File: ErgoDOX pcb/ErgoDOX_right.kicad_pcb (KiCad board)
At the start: 2 copper layers, 182.8 x 158.9 mm, 97 parts, among them J1 AudioJack4, J2 USB_B_Micro, SW0:10 SW0:3, SW0:11 SW0:2, SW0:12 SW0:1, SW0:7 SW0:6, SW0:8 SW0:5, SW0:9 SW0:4, SW1 TS-1187A-B-A-B, SW1:10 SW1:3, SW1:11 SW1:2, SW1:12 SW1:1, SW1:13 SW1:0, SW1:9 SW1:4, SW2:10 SW2:3, SW2:11 SW2:2, SW2:12 SW2:1, SW2:13 SW2:0, SW2:7 SW2:6, SW2:8 SW2:5, SW2:9 SW2:4, SW3:10 SW3:3, SW3:11 SW3:2, SW3:12 SW3:1, SW3:13 SW3:0, SW3:8 SW3:5, SW3:9 SW3:4, SW4:10 SW4:3, SW4:11 SW4:2, SW4:12 SW4:1, SW4:13 SW4:0, SW4:7 SW4:6, SW4:8 SW4:5, SW4:9 SW4:4, SW5:10 SW5:3, SW5:11 SW5:2, SW5:12 SW5:1, SW5:13 SW5:0, SW5:7 SW5:6, SW5:8 SW5:5, SW5:9 SW5:4, U1 ATmega32U4-MU, U2 MCP23018

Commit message: Routed RH board
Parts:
- removed J2: USB_B_Micro, Connectors_USB:USB_Micro-B_Wuerth-629105150521
- removed LED_C1: LED, LEDs:LED_0603
- removed R1, R2: 22, Resistors_SMD:R_0603
- removed R10, R9: 0, Resistors_SMD:R_0603
- removed R8: 1k, Resistors_SMD:R_0603
- removed SW1: TS-1187A-B-A-B, Buttons_Switches_THT:SW_PUSH_6mm
- removed U1: ATmega32U4-MU, Housings_DFN_QFN:QFN-44-1EP_7x7mm_Pitch0.5mm
- added C4: 1u, Capacitors_SMD:C_0603, F.Cu at (128.0, 45.5)
- added C5: 100n, Capacitors_SMD:C_0603, F.Cu at (102.0, 44.5)
- added C6: 100n, Capacitors_SMD:C_0603, F.Cu at (125.5, 35.9)
- moved R7 164.2 mm to (85.0, 44.5)
- moved R6 153.5 mm to (98.3, 44.5)
- moved U2 123.7 mm to (121.9, 42.1), turned to 90 degrees
- moved LED_B1 84.8 mm to (138.3, 35.5), turned to 180 degrees
- moved D2:12 75.7 mm to (175.6, 132.5)
- moved LED_A1 71.4 mm to (138.3, 37.5), turned to 180 degrees
- moved D2:13 70.6 mm to (184.3, 115.5)
- moved D0:12 56.8 mm to (101.3, 158.5), turned to 180 degrees
- moved R3 35.9 mm to (134.3, 37.5), turned to 0 degrees
- moved D0:11 35.4 mm to (101.3, 154.5)
- moved R4 34.9 mm to (134.3, 35.5), turned to 0 degrees
- moved D2:7 13.6 mm to (68.3, 106.5), turned to 0 degrees
- moved D0:8 11.8 mm to (71.3, 133.5), turned to 205 degrees
- moved D0:10 8.54 mm to (101.3, 150.5), turned to 180 degrees
- moved D1:7 6.23 mm to (51.8, 146.8), turned to 25 degrees
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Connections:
- U2 pad 10: /LED_A -> VCC
- U2 pad 11: VCC -> /SCL
- U2 pad 12: /SCL -> /SDA
- U2 pad 13: /SDA -> GND
- U2 pad 14: (no net) -> VCC
- U2 pad 15: GND -> (no net)
- U2 pad 16: VCC -> (no net)
- U2 pad 17: (no net) -> /COL0
- U2 pad 18: (no net) -> /COL1
- U2 pad 19: (no net) -> /COL11
- U2 pad 2: (no net) -> /ROW5
- U2 pad 20: /COL0 -> /COL10
- U2 pad 21: /COL1 -> /COL4
- U2 pad 22: /COL11 -> /COL5
- U2 pad 23: /COL10 -> /COL6
- U2 pad 24: /COL4 -> (no net)
- U2 pad 3: /ROW5 -> /ROW4
- U2 pad 4: /ROW4 -> /ROW3
- U2 pad 5: /ROW3 -> /ROW2
- U2 pad 6: /ROW2 -> /ROW1
- U2 pad 7: /ROW1 -> /ROW0
- U2 pad 8: /ROW0 -> /LED_B
- U2 pad 9: /LED_B -> /LED_A
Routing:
- net /COL1: track 0.00 -> 225.4 mm
- net /COL10: track 0.00 -> 183.7 mm
- net /COL6: track 0.00 -> 181.3 mm
- net /COL4: track 0.00 -> 170.9 mm
- net /COL11: track 0.00 -> 156.6 mm
- net /COL0: track 0.00 -> 151.8 mm
- net /COL5: track 0.00 -> 131.5 mm
- net /ROW1: track 156.2 -> 250.1 mm
- net VCC: track 0.00 -> 76.9 mm, vias 0 -> 2
- net /ROW3: track 91.5 -> 165.2 mm
- net Net-(D0:12-Pad2): track 0.90 -> 62.1 mm
- net /ROW4: track 121.7 -> 179.9 mm
- net Net-(D0:11-Pad2): track 0.00 -> 45.4 mm
- net /SCL: track 0.00 -> 43.6 mm, vias 0 -> 1
- net /ROW0: track 269.4 -> 231.0 mm, vias 1 -> 0
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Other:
- board size 182.8 x 158.9 mm -> 182.8 x 157.1 mm
- board text removed: "LEFT HAND"
- board text removed: "ProfetKeyboards.com"
- board text removed: "RIGHT HAND"

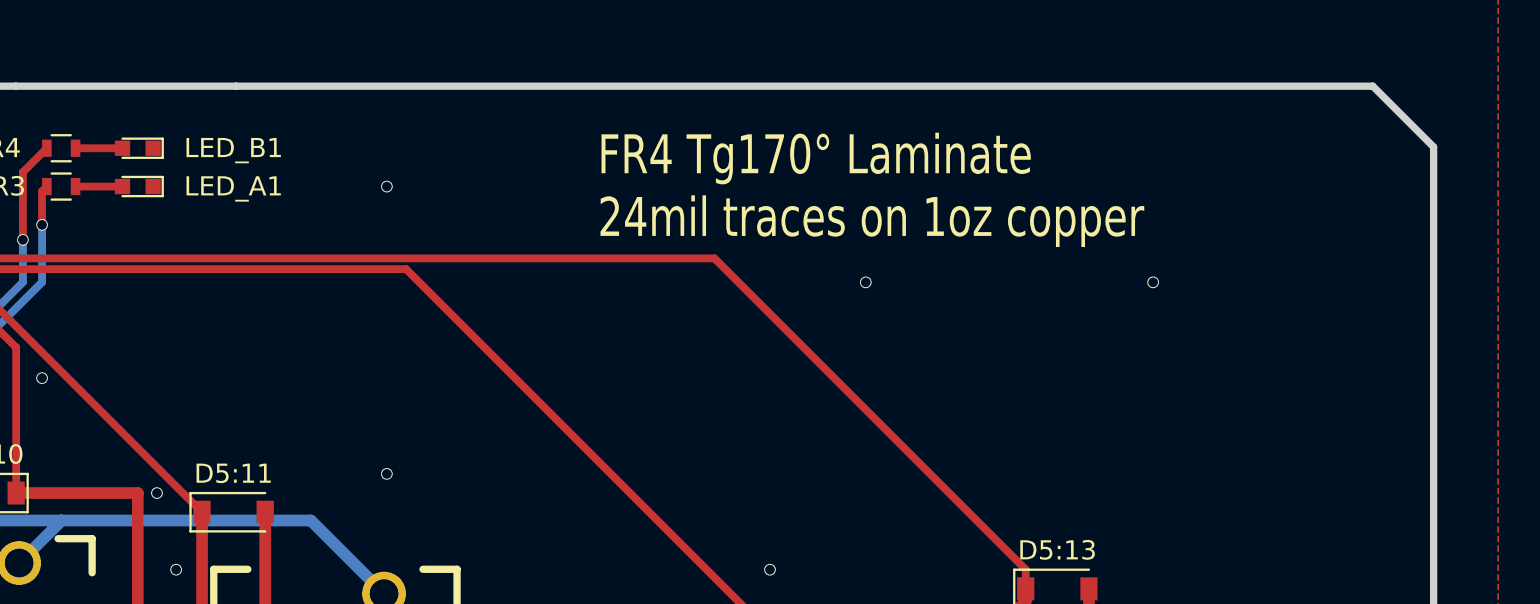
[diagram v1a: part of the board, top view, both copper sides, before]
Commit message: Added revision, generated gerbers
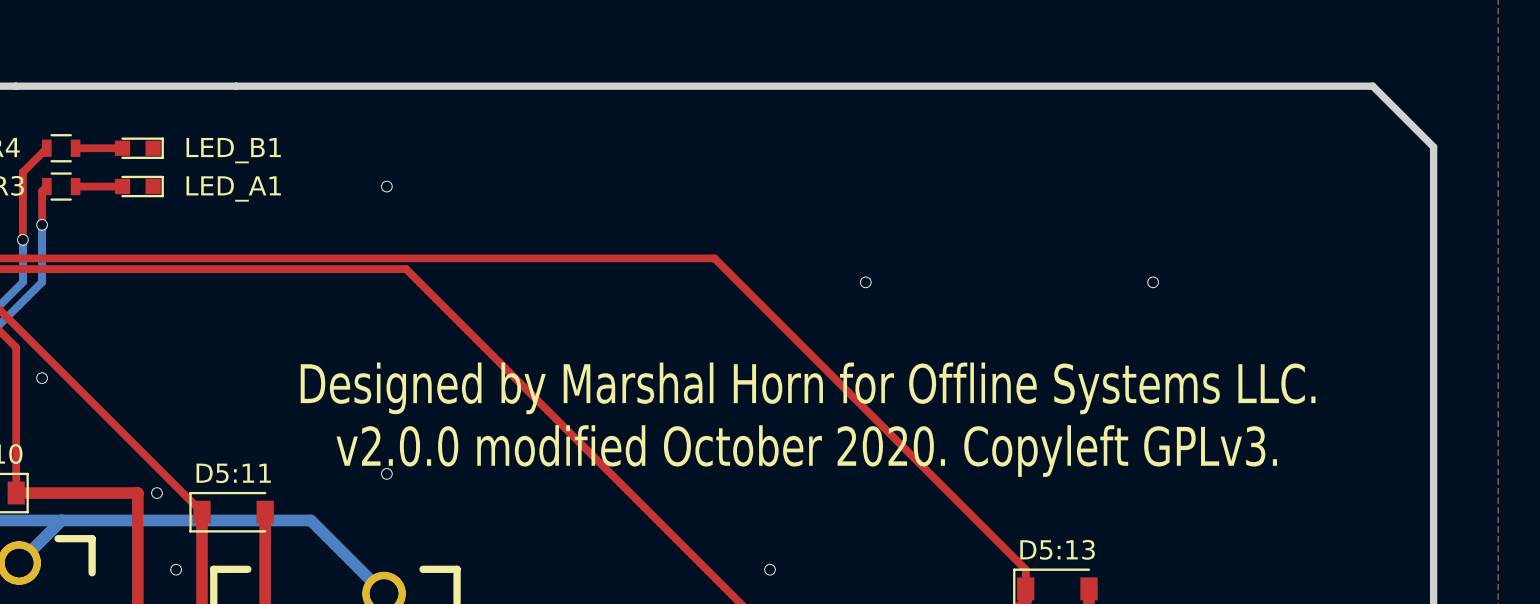
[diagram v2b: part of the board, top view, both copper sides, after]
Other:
- rule pad_to_mask_clearance: 0.0508 -> 0
- board text added: "Designed by Marshal Horn for Offline Systems LLC. v2.0.0 modified October 2020. Copyleft GPLv3."
- board text removed: "FR4 Tg170° Laminate 24mil traces on 1oz copper"
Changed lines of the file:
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@@
   (general
     (thickness 1.6002)
-    (drawings 22)
+    (drawings 21)
     (tracks 467)
     (zones 0)
@@
   )
   (page A4)
+  (title_block
+    (title "ErgoDox Right PCB")
+    (date 2020-10-12)
+    (rev 2.0.0)
+    (company "Offline Systems")
+  )
   (layers
     (0 Front signal)
@@
     (pad_size 0.8 0.8)
     (pad_drill 0.5)
-    (pad_to_mask_clearance 0.0508)
-    (solder_mask_min_width 0.101)
+    (pad_to_mask_clearance 0)
     (aux_axis_origin 0 0)
     (grid_origin 176.276 47.498)
     (visible_elements 7FFFFF7F)
     (pcbplotparams
-      (layerselection 0x01fff_ffffffff)
+      (layerselection 0x0dfff_ffffffff)
       (usegerberextensions true)
       (usegerberattributes true)
       (usegerberadvancedattributes true)
       (creategerberjobfile true)
-      (excludeedgelayer true)
+      (excludeedgelayer false)
       (linewidth 0.150000)
       (plotframeref false)
@@
       (drillshape 0)
       (scaleselection 1)
-      (outputdirectory "gerber/"))
+      (outputdirectory "gerber_right/"))
   )
   (net 0 "")
@@
     )
   )
+  (gr_text "Designed by Marshal Horn for Offline Systems LLC.\nv2.0.0 modified October 2020. Copyleft GPLv3." (at 173.276 49.498) (layer F.SilkS)
+    (effects (font (size 2.032 1.524) (thickness 0.3048)))
+  )
   (gr_line (start 90.121 32.258) (end 93.521 32.258) (layer Edge.Cuts) (width 0.381))
   (gr_line (start 90.121 32.258) (end 77.8764 32.258) (layer Edge.Cuts) (width 0.381))
@@
     (effects (font (size 8.128 12.192) (thickness 2.032)) (justify mirror))
   )
-  (gr_text "FR4 Tg170° Laminate\n24mil traces on 1oz copper " (at 189.276 37.498) (layer B.SilkS)
-    (effects (font (size 2.032 1.524) (thickness 0.3048)) (justify left mirror))
-  )
-  (gr_text "FR4 Tg170° Laminate\n24mil traces on 1oz copper " (at 162.276 37.498) (layer F.SilkS)
-    (effects (font (size 2.032 1.524) (thickness 0.3048)) (justify left))
-  )
   (gr_line (start 127.1524 152.908) (end 196.3928 152.908) (angle 90) (layer Edge.Cuts) (width 0.381))

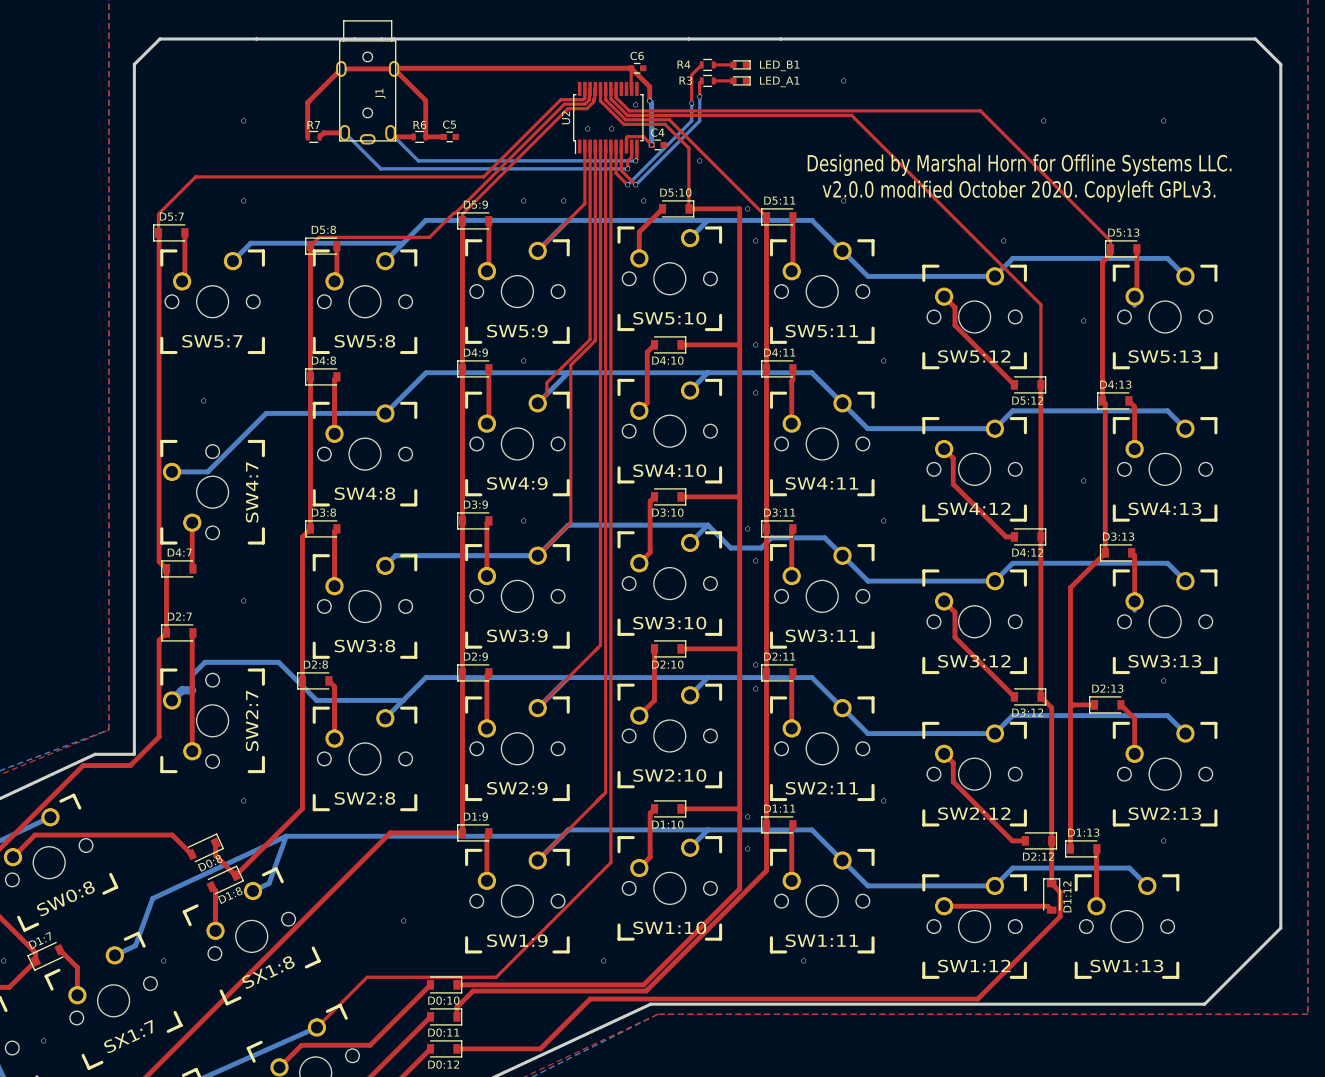
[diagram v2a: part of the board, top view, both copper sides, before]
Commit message: Switched MCP23018 to SOIC package
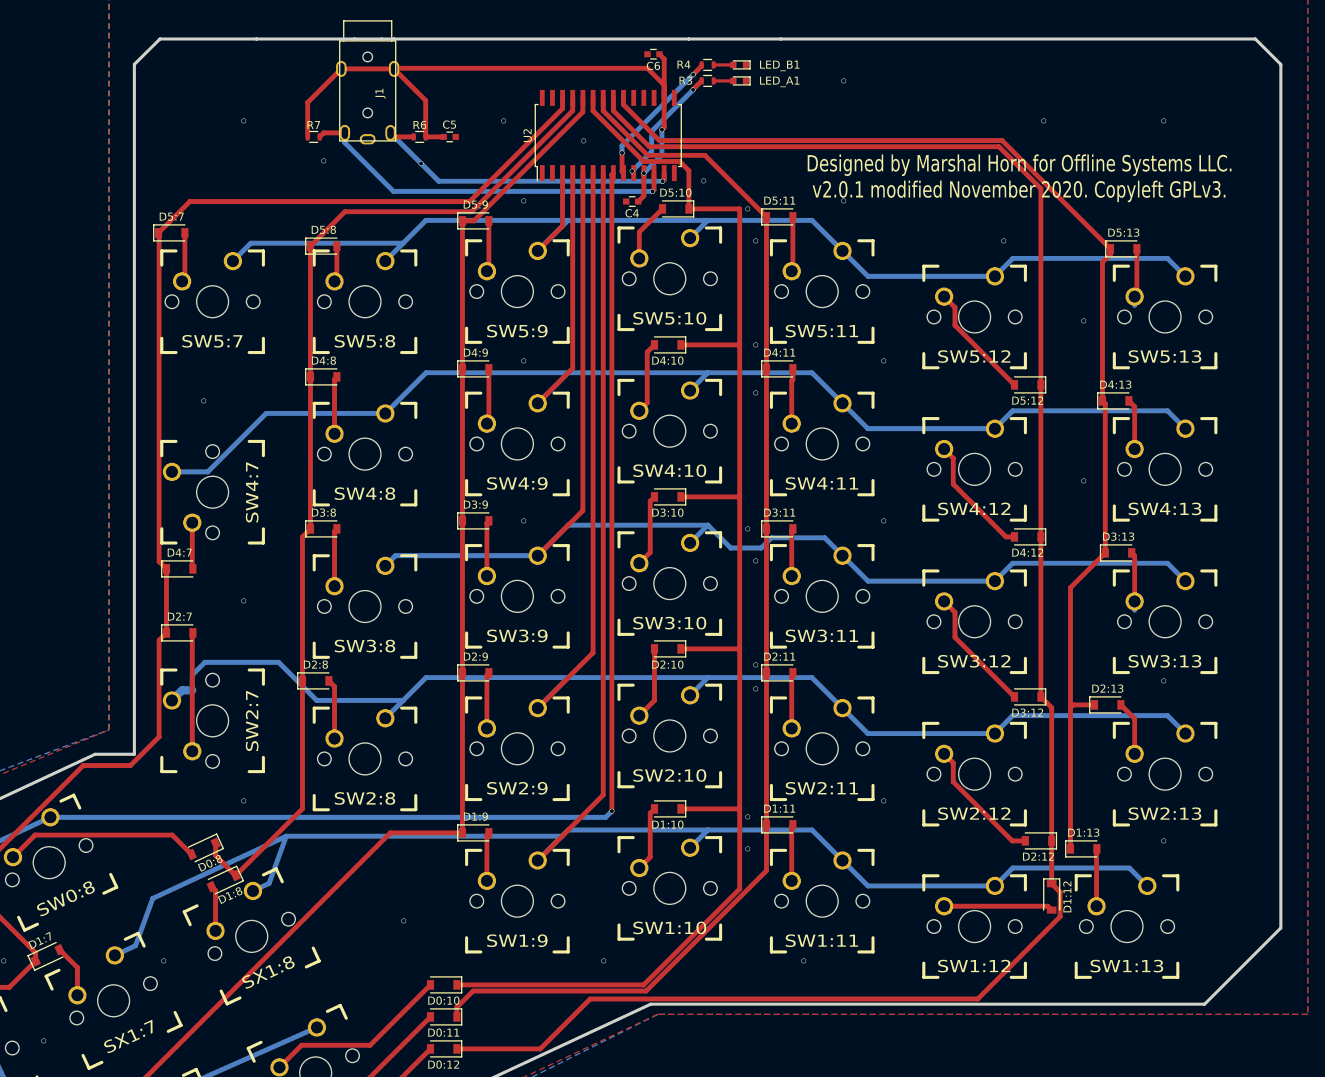
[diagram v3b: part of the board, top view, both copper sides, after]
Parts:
- U2: footprint Housings_SSOP:SSOP-24_5.3x8.2mm_Pitch0.65mm -> Housings_SOIC:SOIC-28W_7.5x17.9mm_Pitch1.27mm
- moved C4 7.76 mm to (124.8, 52.6), turned to 180 degrees
- moved C6 2.68 mm to (127.5, 34.2), turned to 180 degrees
- moved U2 2.23 mm to (121.9, 44.3)
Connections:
- U2 pad 10: VCC -> /LED_A
- U2 pad 11: /SCL -> VCC
- U2 pad 12: /SDA -> /SCL
- U2 pad 13: GND -> /SDA
- U2 pad 14: VCC -> (no net)
- U2 pad 15: (no net) -> GND
- U2 pad 16: (no net) -> VCC
- U2 pad 17: /COL0 -> (no net)
- U2 pad 18: /COL1 -> (no net)
- U2 pad 19: /COL11 -> (no net)
- U2 pad 2: /ROW5 -> (no net)
- U2 pad 20: /COL10 -> /COL0
- U2 pad 21: /COL4 -> /COL1
- U2 pad 22: /COL5 -> /COL11
- U2 pad 23: /COL6 -> /COL10
- U2 pad 24: (no net) -> /COL4
- U2 pad 3: /ROW4 -> /ROW5
- U2 pad 4: /ROW3 -> /ROW4
- U2 pad 5: /ROW2 -> /ROW3
- U2 pad 6: /ROW1 -> /ROW2
- U2 pad 7: /ROW0 -> /ROW1
- U2 pad 8: /LED_B -> /ROW0
- U2 pad 9: /LED_A -> /LED_B
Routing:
- net /ROW0: track 231.0 -> 246.5 mm, vias 0 -> 1
- net VCC: track 76.9 -> 85.5 mm
- net /COL1: track 225.4 -> 233.3 mm
- net /LED_B: track 24.2 -> 17.7 mm
- net /LED_A: track 22.0 -> 15.6 mm
- net /ROW1: track 250.1 -> 245.5 mm
- net /COL6: track 181.3 -> 176.8 mm
- net /ROW5: track 153.1 -> 148.6 mm
- net /SCL: track 43.6 -> 47.9 mm
- net /ROW4: track 179.9 -> 175.7 mm
- net /ROW2: track 223.2 -> 219.1 mm
- net /ROW3: track 165.2 -> 161.2 mm
- net /SDA: track 37.1 -> 40.7 mm, vias 1 -> 2
- net /COL5: track 131.5 -> 129.0 mm
- net /COL4: track 170.9 -> 168.6 mm
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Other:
- board text added: "Designed by Marshal Horn for Offline Systems LLC. v2.0.1 modified November 2020. Copyleft GPLv3."
- board text removed: "Designed by Marshal Horn for Offline Systems LLC. v2.0.0 modified October 2020. Copyleft GPLv3."
